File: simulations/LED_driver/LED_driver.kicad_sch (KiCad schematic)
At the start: 7 parts, among them Q2 NPN, U1 ${SIM.PARAMS}, U2 TL082

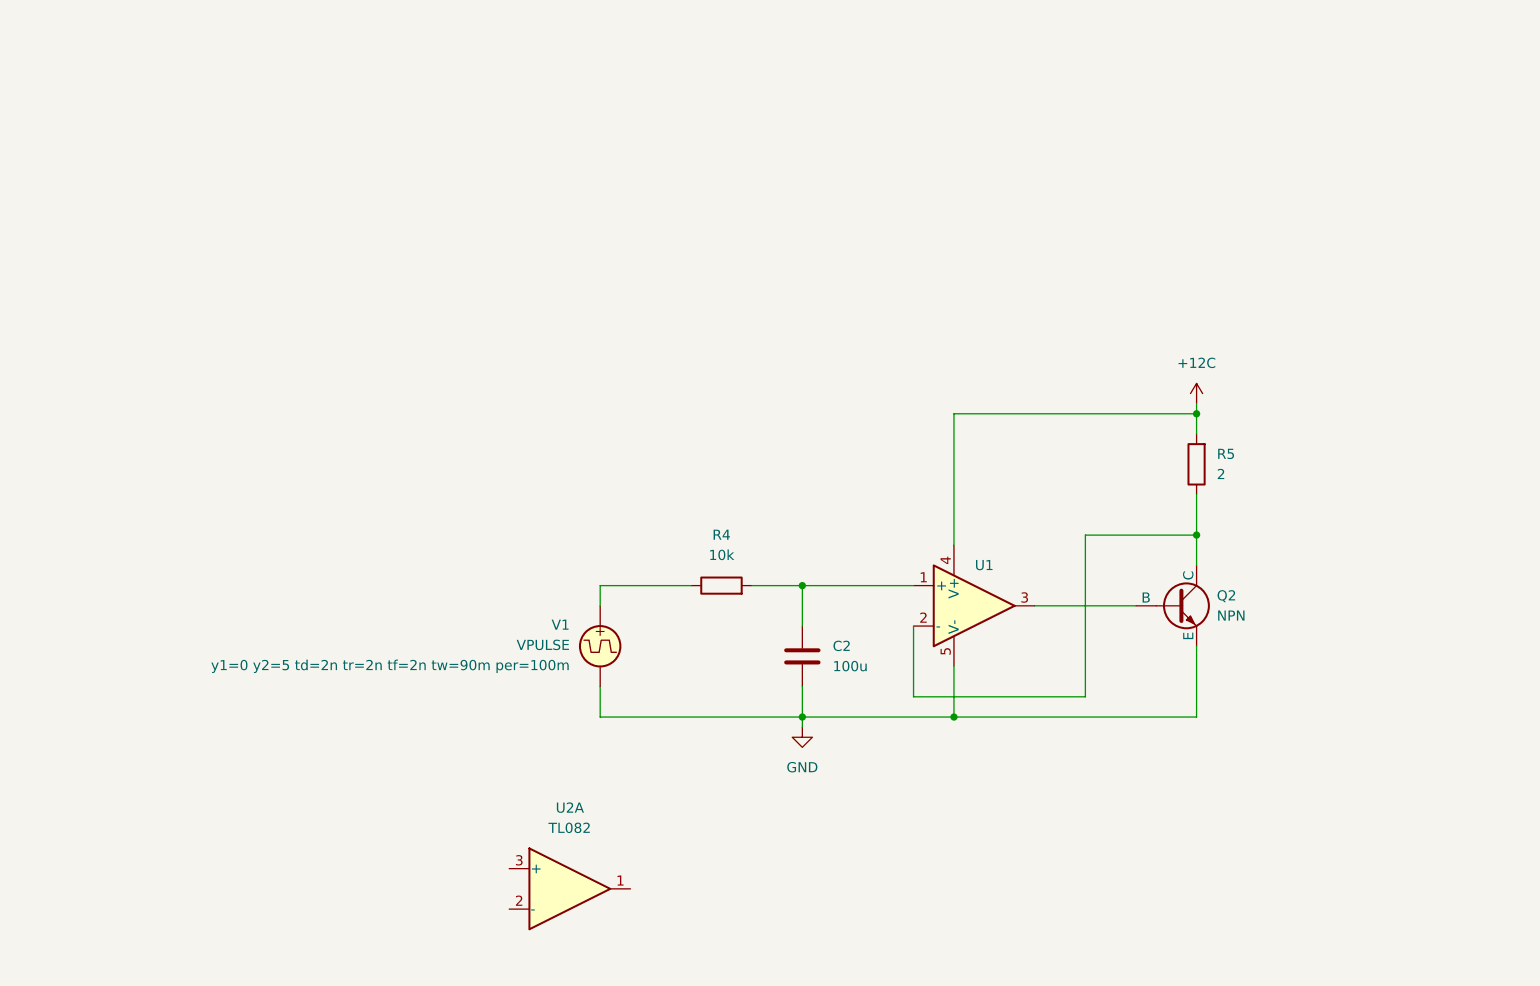
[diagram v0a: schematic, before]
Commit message: Improve LED simulation
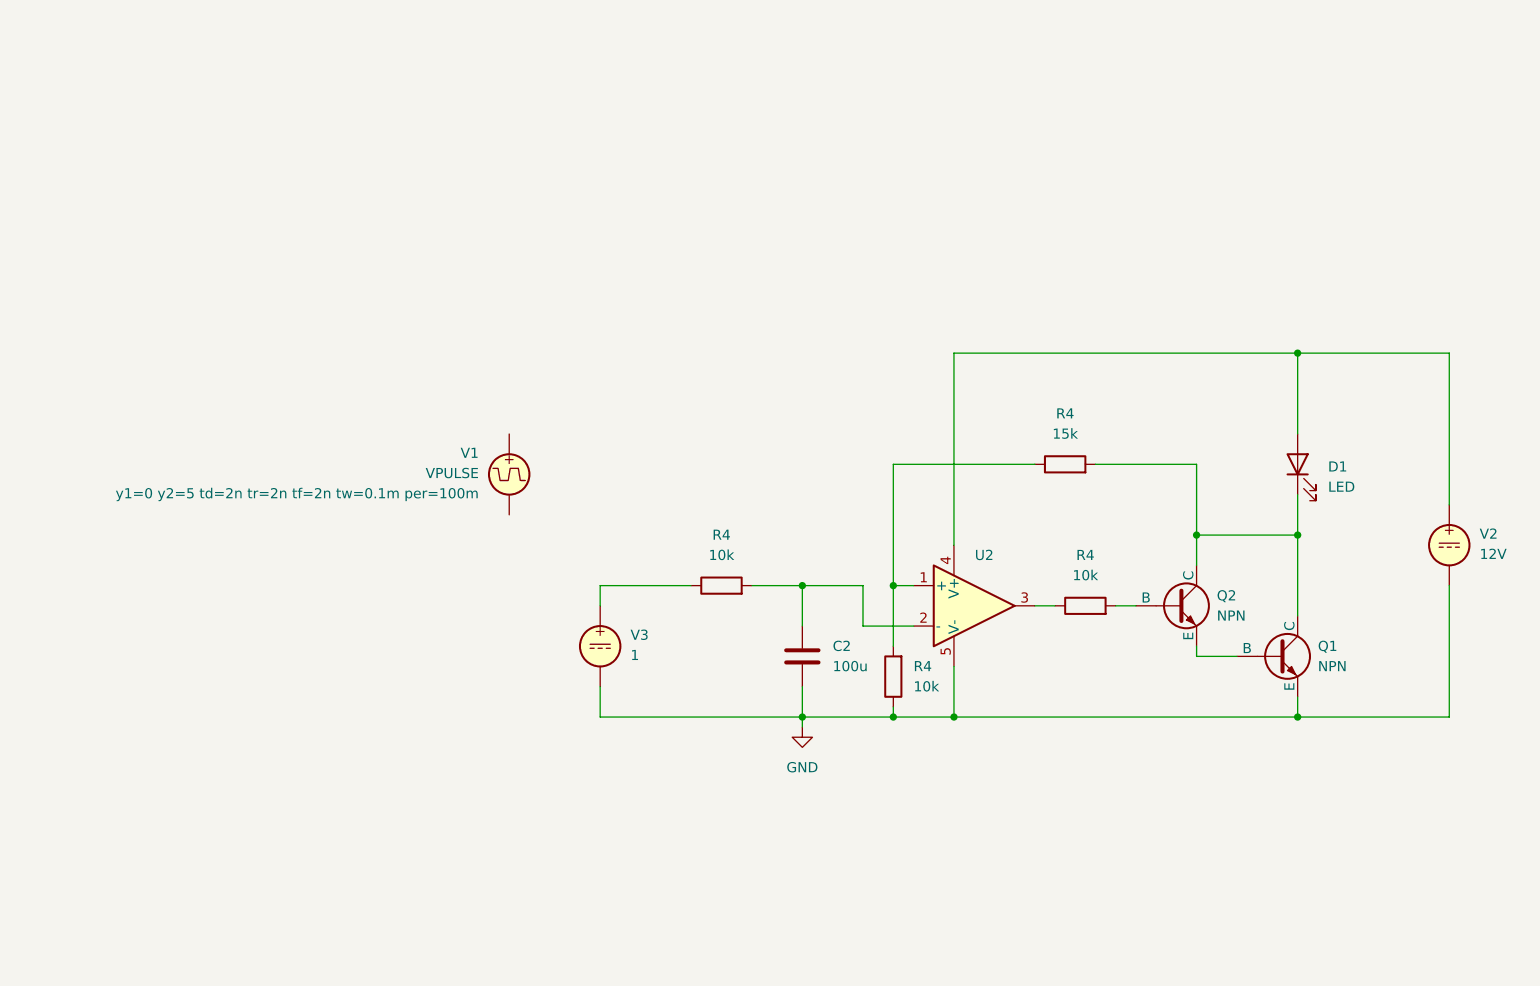
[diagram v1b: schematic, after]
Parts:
- removed R5: 2, symbol Device:R
- removed U1: ${SIM.PARAMS}, symbol Simulation_SPICE:OPAMP
- removed U2: TL082, symbol Amplifier_Operational:TL082
- added D1: LED, symbol Device:LED
- added Q1: NPN, symbol Simulation_SPICE:NPN
- added R4 (x2): 10k, symbol Device:R
- added R4: 15k, symbol Device:R
- added U2: ${SIM.PARAMS}, symbol Simulation_SPICE:OPAMP
- added V2: 12V, symbol Simulation_SPICE:VDC
- added V3: 1, symbol Simulation_SPICE:VDC
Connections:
- net GND: now also Q1.3 (E), R4.1, U2.5 (V-), V2.2, V3.2; no longer Q2.3 (E), V1.2
- net at Q2.1 (C): now also D1.1 (K), Q1.1 (C), R4.2
- net at Q2.2 (B): now also R4.2
- net at V1.1: no longer R4.1
- net at C2.1, R4.2: now also U2.2 (-)
- new net: Q1.2 (B), Q2.3 (E)
- new net: D1.2 (A), U2.4 (V+), V2.1
- new net: R4.1, R4.2, U2.1 (+)
- new net: R4.1, U2.3
- new net: R4.1, V3.1
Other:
- moved on the sheet: V1

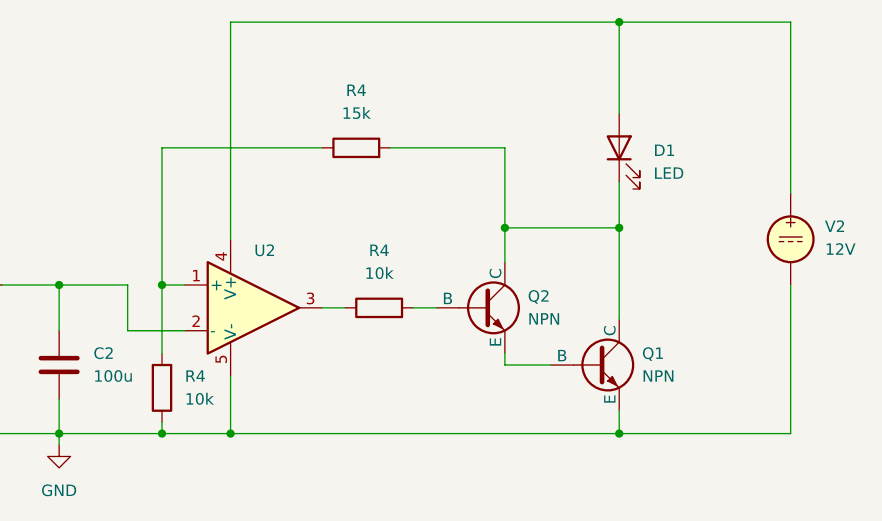
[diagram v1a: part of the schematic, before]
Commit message: Switch to MOSFET transistor
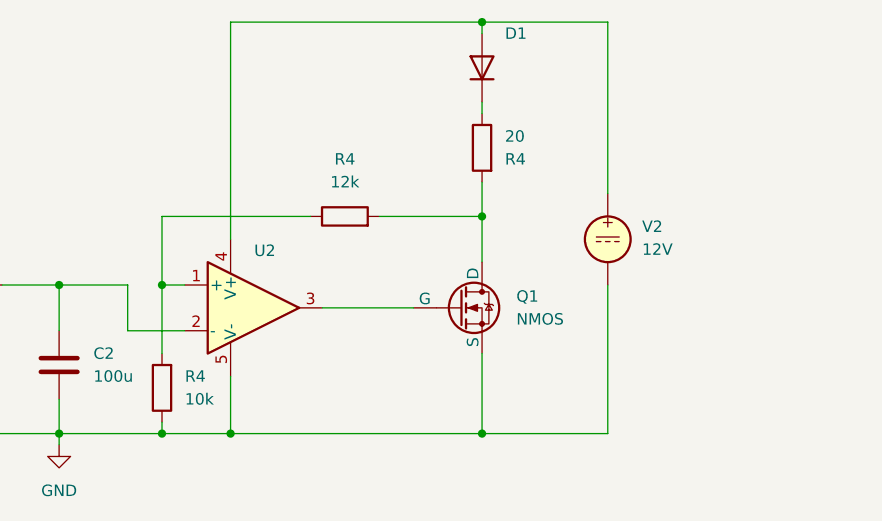
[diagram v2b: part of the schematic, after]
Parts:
- removed D1: LED, symbol Device:LED
- removed Q1, Q2: NPN, symbol Simulation_SPICE:NPN
- added D1: D, symbol Simulation_SPICE:D
- added Q1: NMOS, symbol Simulation_SPICE:NMOS
- R4: value 10k -> 20
- R4: value 15k -> 12k
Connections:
- net GND: now also Q1.3 (S)
- net at R4.2: now also R4.2, Q1.1 (D)
- net at U2.4 (V+), V2.1: now also D1.2 (A)
- net at R4.1: now also D1.1 (K); no longer U2.3
- new net: Q1.2 (G), U2.3
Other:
- moved on the sheet: R4, V2

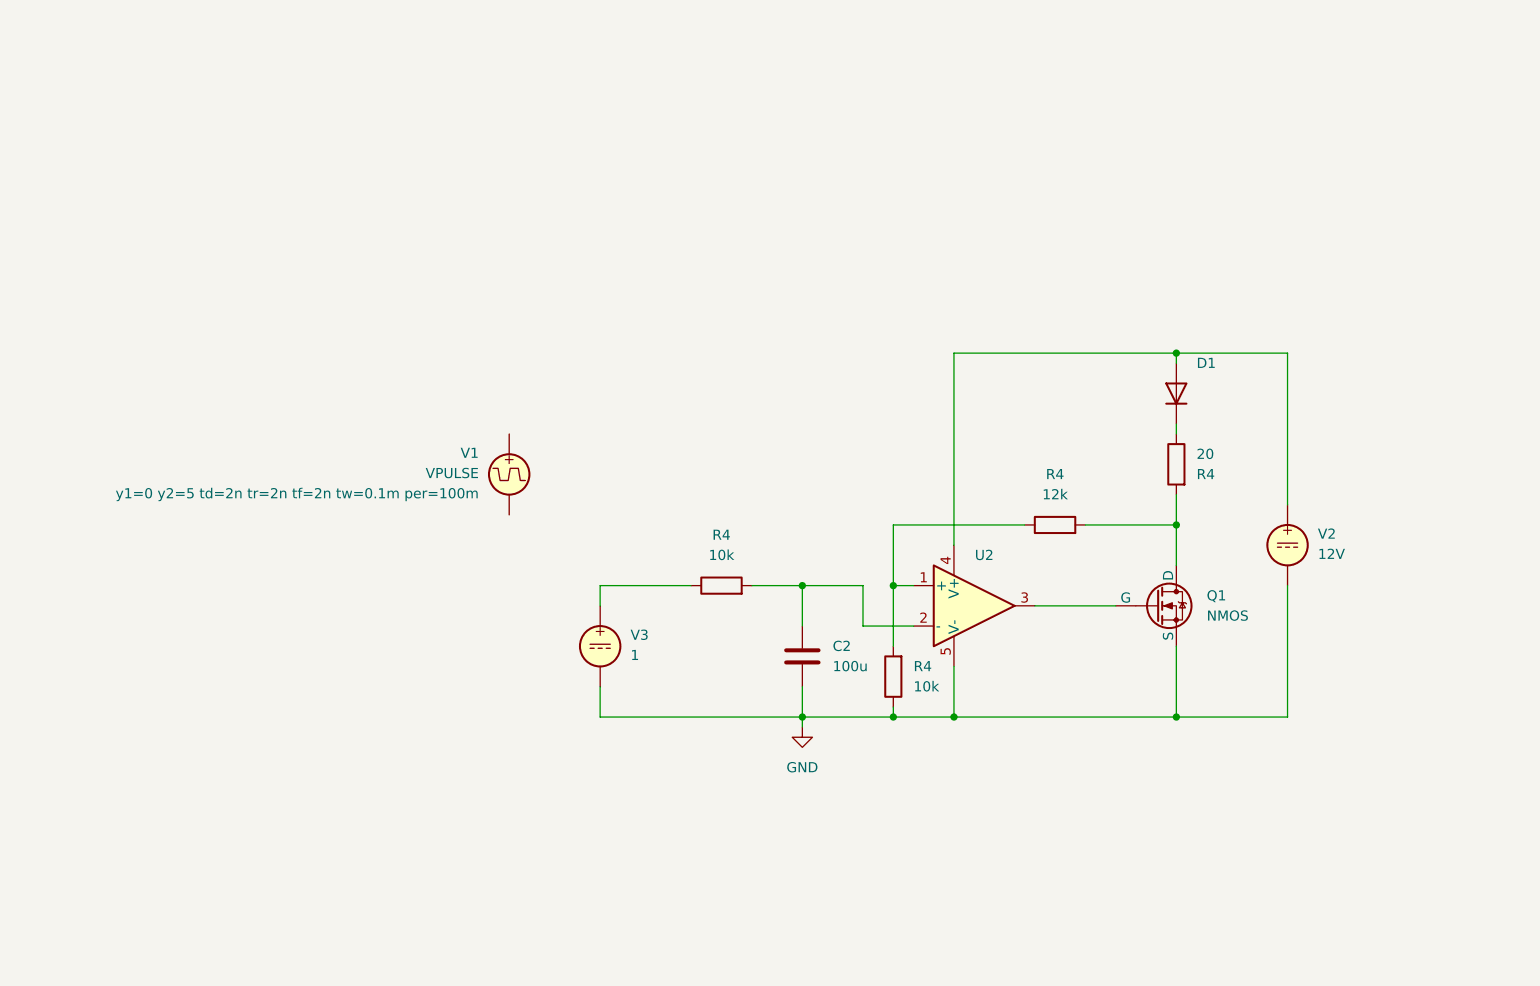
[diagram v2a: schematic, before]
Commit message: Add another, experimental LED controller
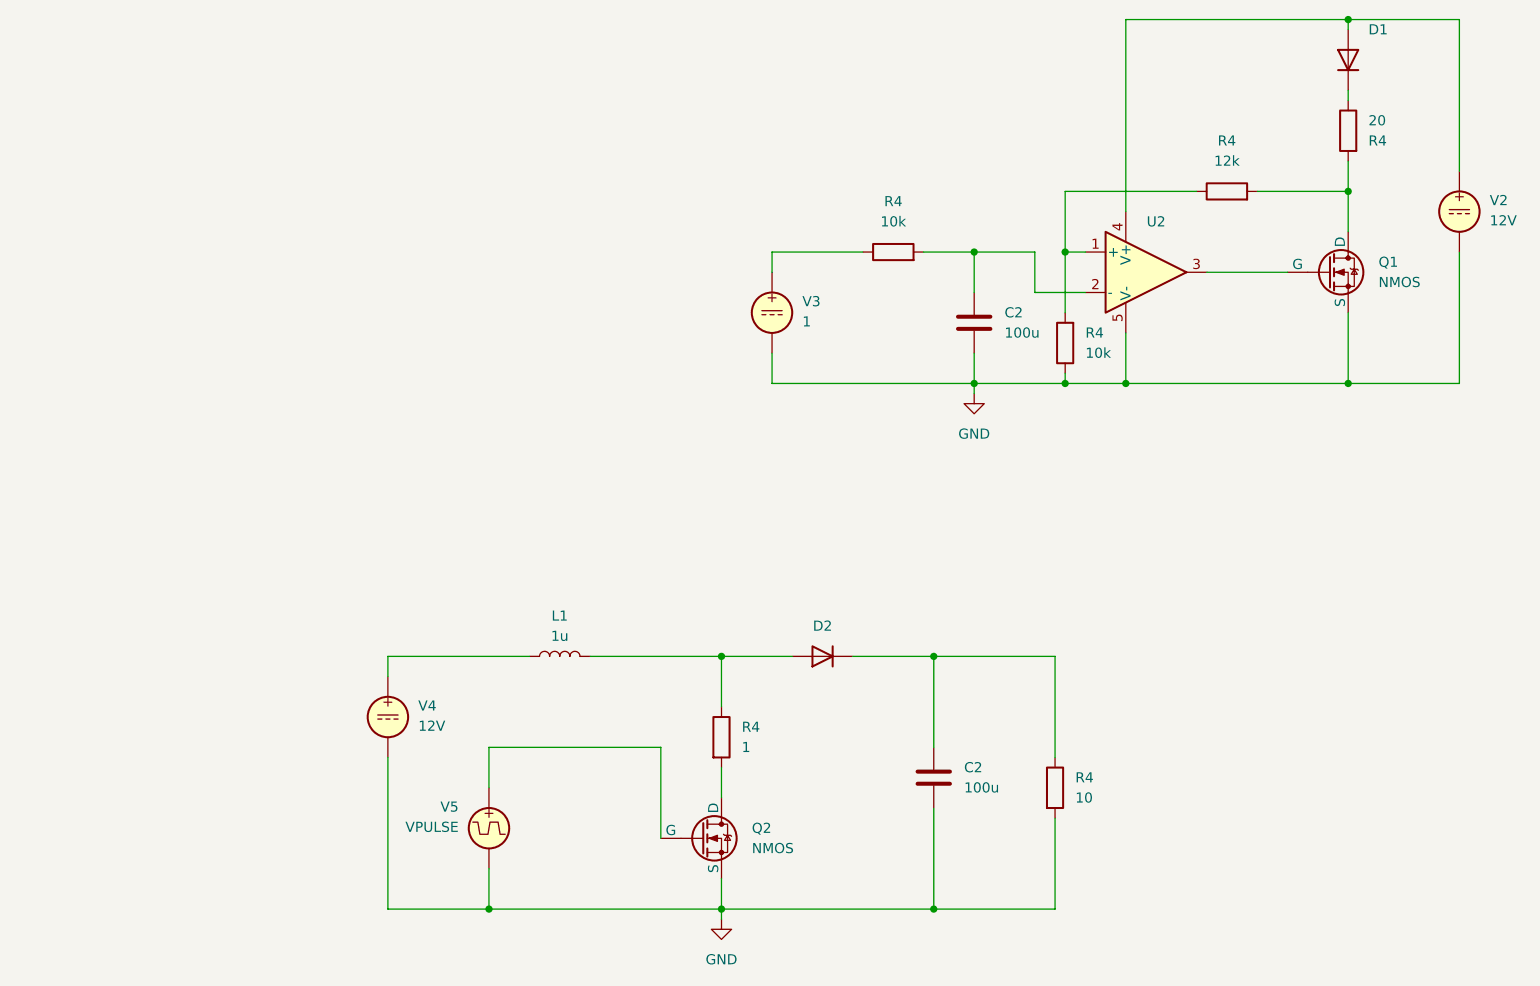
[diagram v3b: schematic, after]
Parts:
- removed V1: VPULSE, symbol Simulation_SPICE:VPULSE
- added C2: 100u, symbol Device:C
- added D2: D, symbol Simulation_SPICE:D
- added L1: 1u, symbol Device:L
- added Q2: NMOS, symbol Simulation_SPICE:NMOS
- added R4: 1, symbol Device:R
- added R4: 10, symbol Device:R
- added V4: 12V, symbol Simulation_SPICE:VDC
- added V5: VPULSE, symbol Simulation_SPICE:VPULSE
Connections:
- net GND: now also C2.2, Q2.3 (S), R4.2, V4.2, V5.2
- new net: L1.1, V4.1
- new net: C2.1, D2.1 (K), R4.1
- new net: Q2.2 (G), V5.1
- new net: D2.2 (A), L1.2, R4.1
- new net: Q2.1 (D), R4.2
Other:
- moved on the sheet: C2, D1, Q1, R4, U2, V2, V3
